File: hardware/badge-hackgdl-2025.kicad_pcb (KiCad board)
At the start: 11 copper layers, 73.4 x 79.5 mm, 63 parts, among them J1 ADDON, J2 Battery, P1 USB_C_Plug_USB2.0, Q1 DMG3415U-7, Q2 MMBT2222A, SW1 ON, SW2 RESET, SW3 BOOT, SW4 RIGHT, SW5 BACK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

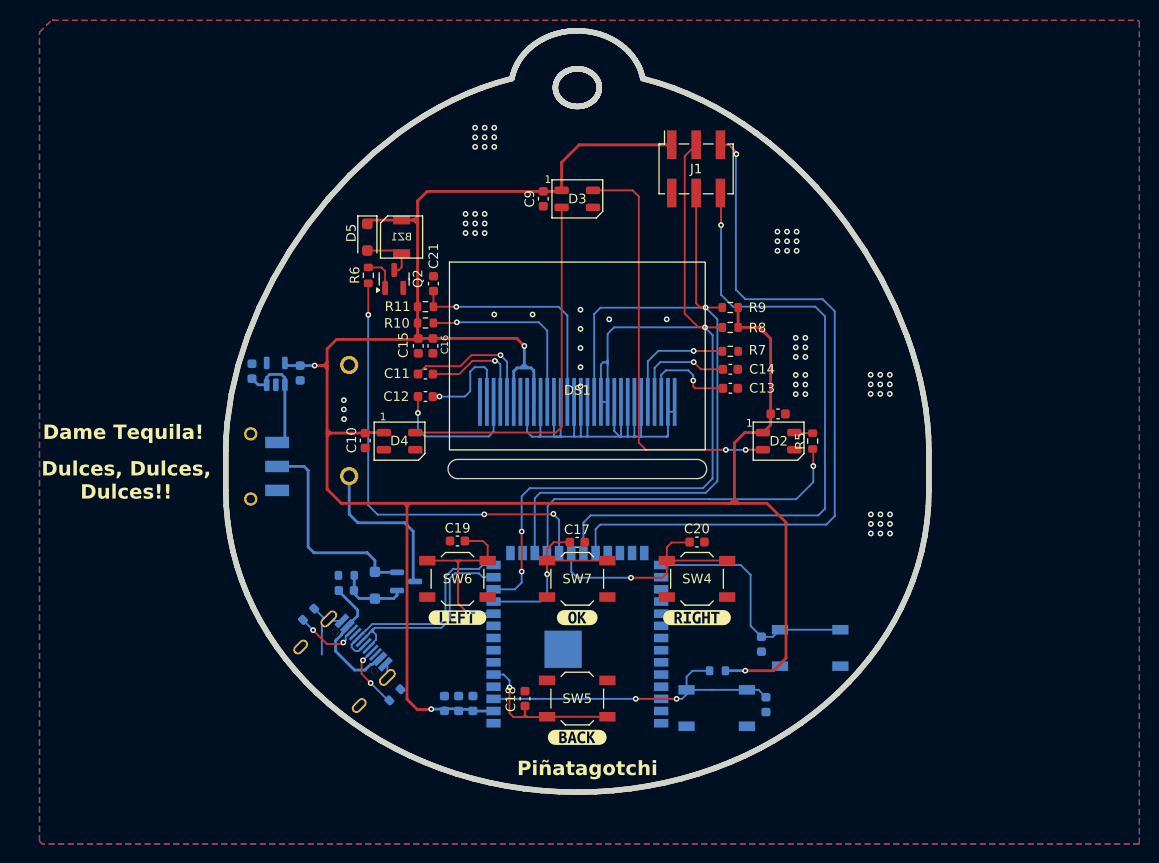
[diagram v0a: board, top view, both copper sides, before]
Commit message: feat(hw): update button
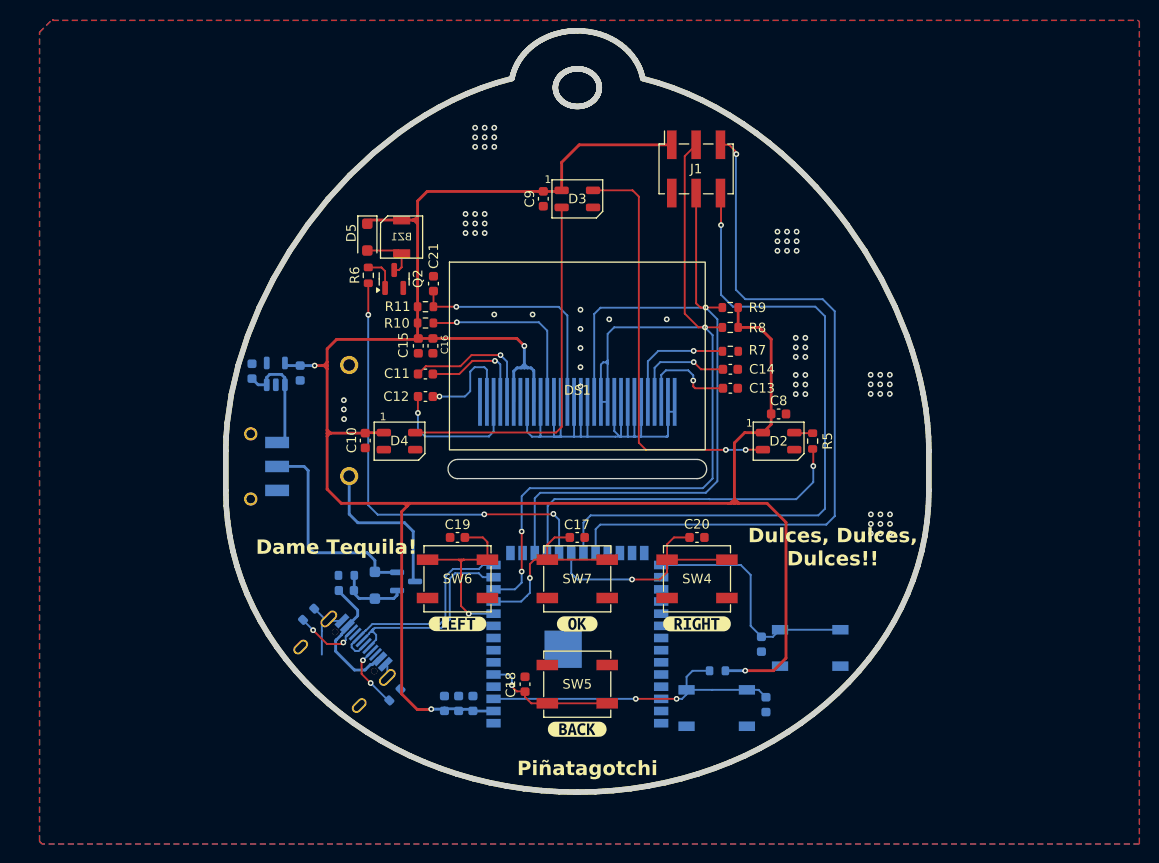
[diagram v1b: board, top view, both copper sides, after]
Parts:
- SW4, SW5, SW6, SW7: footprint Button_Switch_SMD:SW_SPST_TL3342 -> Footprints:Button_6.6x6.5
- moved C18 1.50 mm to (128.2, 87.1)
- moved SW5 1.50 mm to (133.7, 87.1)
- moved kibuzzard-6789895F 0.85 mm to (133.7, 91.8)
- moved kibuzzard-678830ED 0.65 mm to (121.2, 80.8)
- moved kibuzzard-678830F7 0.65 mm to (146.2, 80.8)
- moved kibuzzard-67898922 0.65 mm to (133.7, 80.8)
- moved C17 0.51 mm to (133.7, 71.8)
- moved C20 0.48 mm to (146.2, 71.8)
- moved C19 0.37 mm to (121.2, 71.8)
- moved C8 0.06 mm to (154.7, 58.9)
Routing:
- net /BACK: track 17.6 -> 14.0 mm
- net /RIGHT: track 24.0 -> 24.5 mm
- net +3V3: track 241.4 -> 242.0 mm
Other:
- board text added: "Badge HackGDL 2025 v2.1"
- board text removed: "Badge HackGDL 2025 v2.0"

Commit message: feat(hw): add 3d model for pcb
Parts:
- added Ref** (x2): Val**, Footprints:badge-hackgdl-2025-Edge_Cuts, F.Cu at (133.7, 58.6)
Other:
- outline, holes or cut-outs redrawn

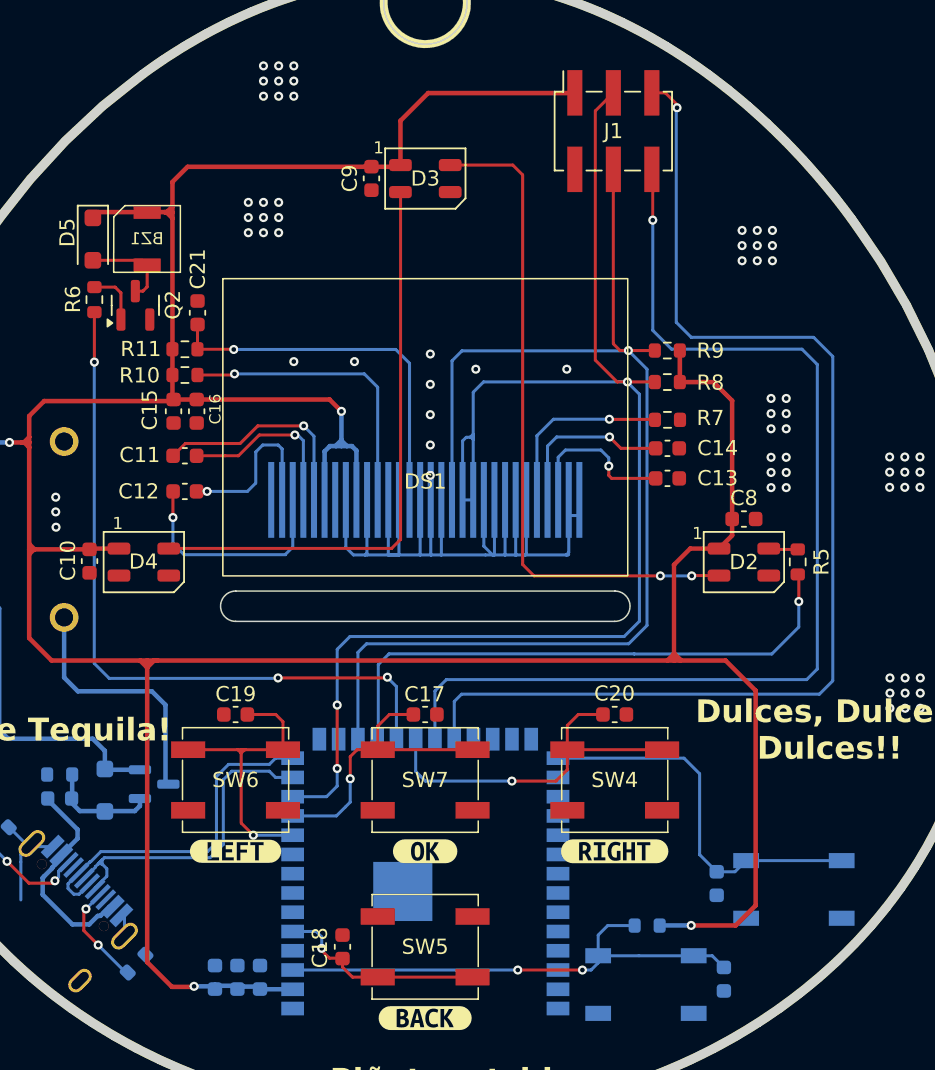
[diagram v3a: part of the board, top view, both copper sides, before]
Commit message: refactor(hw): change routes width
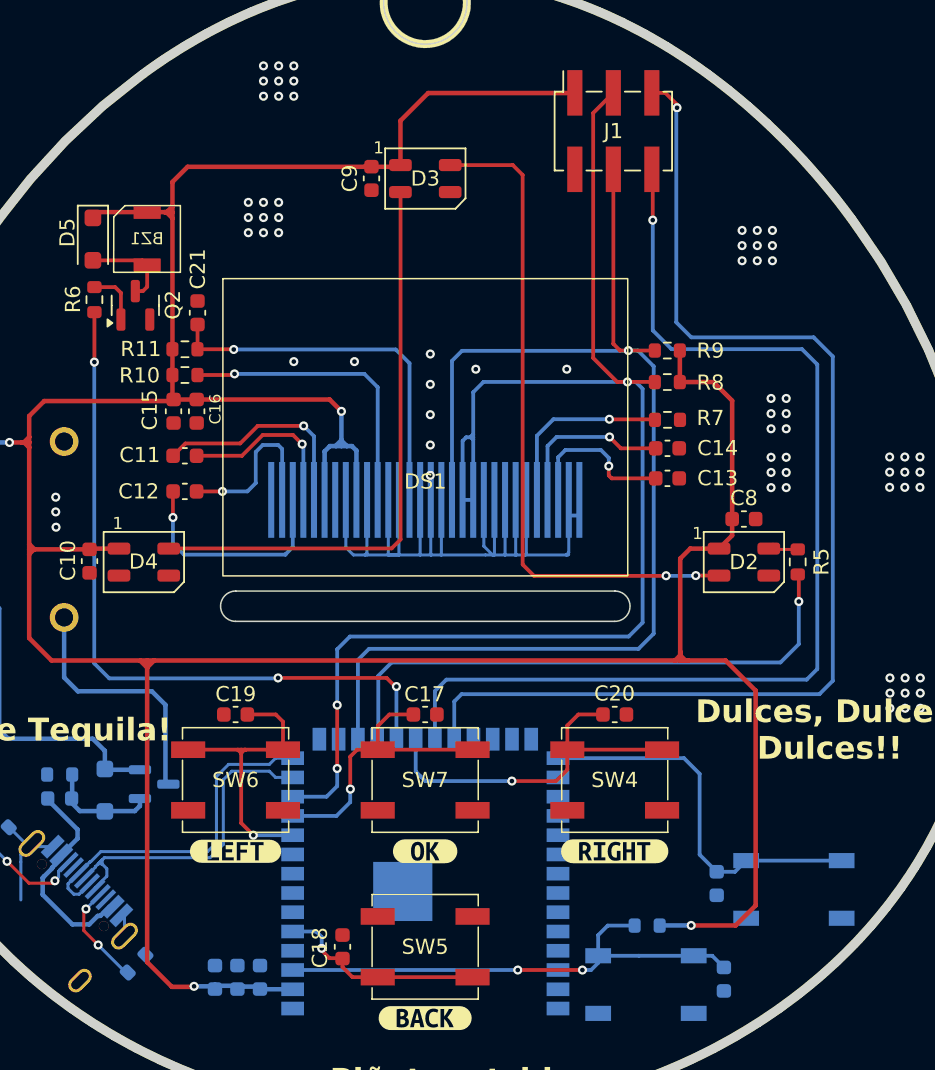
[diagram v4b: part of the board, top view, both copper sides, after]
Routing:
- net /SCL: track 79.7 -> 80.7 mm
- net /SDA: track 95.1 -> 95.9 mm

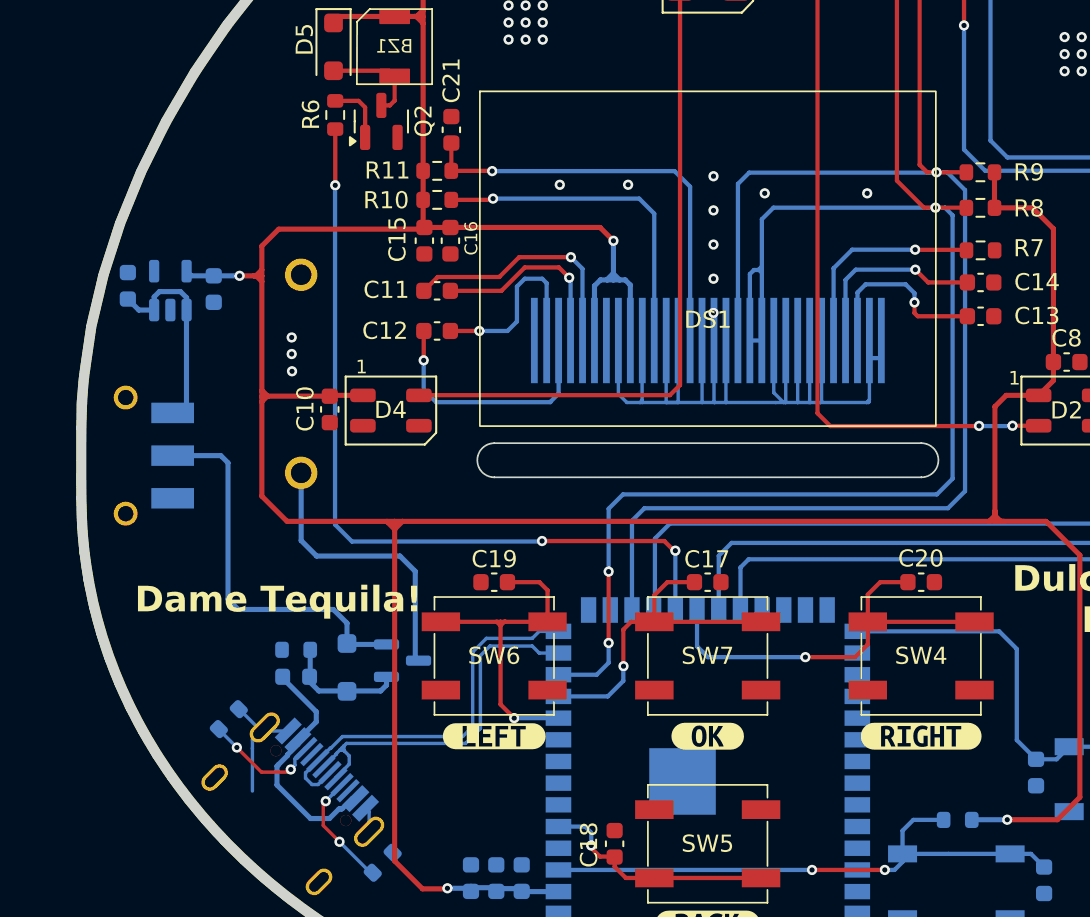
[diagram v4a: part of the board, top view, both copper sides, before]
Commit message: refactor(hw): switch approached the edge of the pcb
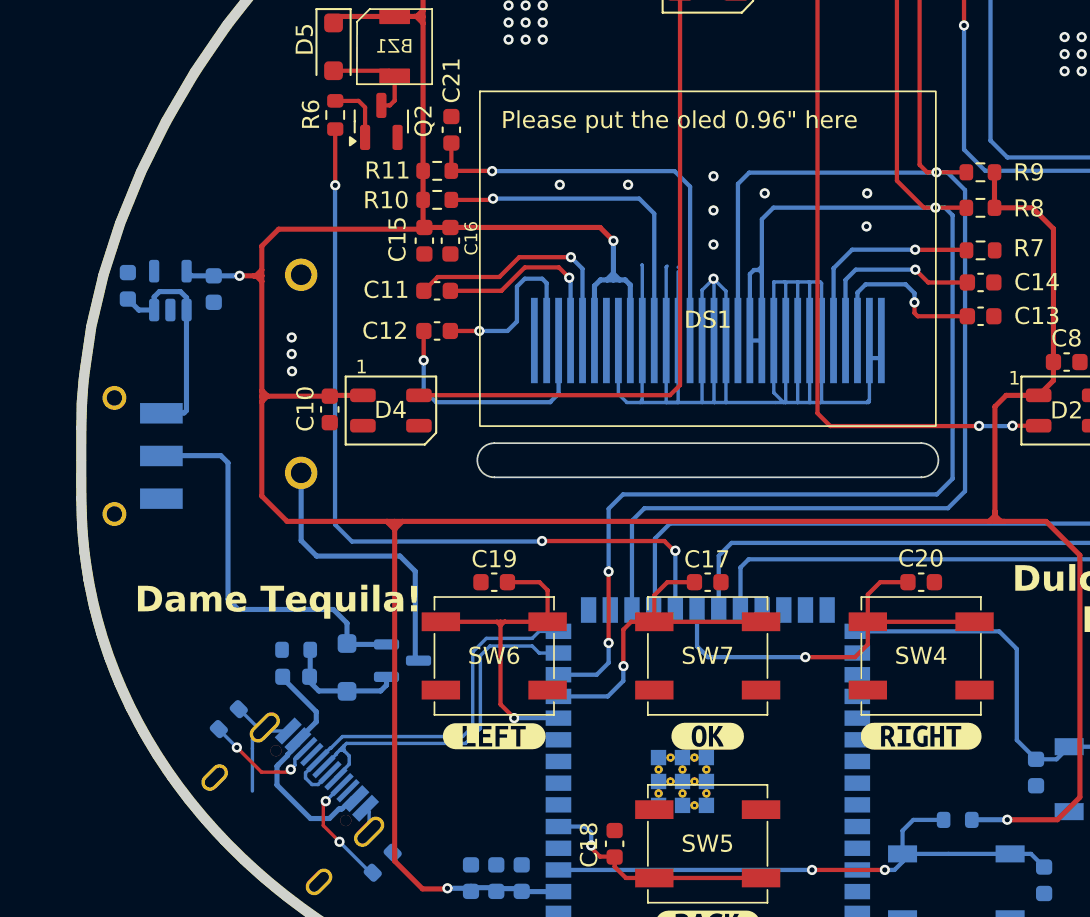
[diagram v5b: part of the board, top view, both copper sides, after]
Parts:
- U2: value ESP32-S3-WROOM-1-N16 -> ESP32-S3-WROOM-1-N4
- moved SW1 0.66 mm to (100.7, 64.4)
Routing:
- net GND: track 83.0 -> 117.2 mm
- net Net-(SW1-A): track 12.2 -> 12.9 mm
- net Net-(D1-K): track 22.5 -> 23.1 mm
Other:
- board text added: "Please put the oled 0.96{dblquote} here"

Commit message: fix(hw): add GND path and change the oled footprint side
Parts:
- DS1: moved to B.Cu
- moved DS1 0.06 mm to (133.6, 56.9), turned to 180 degrees
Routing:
- net GND: vias 69 -> 73
